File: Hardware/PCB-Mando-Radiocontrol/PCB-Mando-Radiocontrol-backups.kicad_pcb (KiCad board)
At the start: 2 copper layers, 132 x 66 mm, 25 parts, among them J1 USB 2.0 a UART TTL 6 pines CP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, J2 ALIMENTACION, SW1 SW_SPDT, SW2 SW_SPDT, SW3 SW_SPDT, U1 ATMEGA328P, U2 Nrf24l01, U3 AMS1117-3.3, U4 AMS1117-5.0, U5 COM-09032, U6 COM-09032, Y1 16MHZ

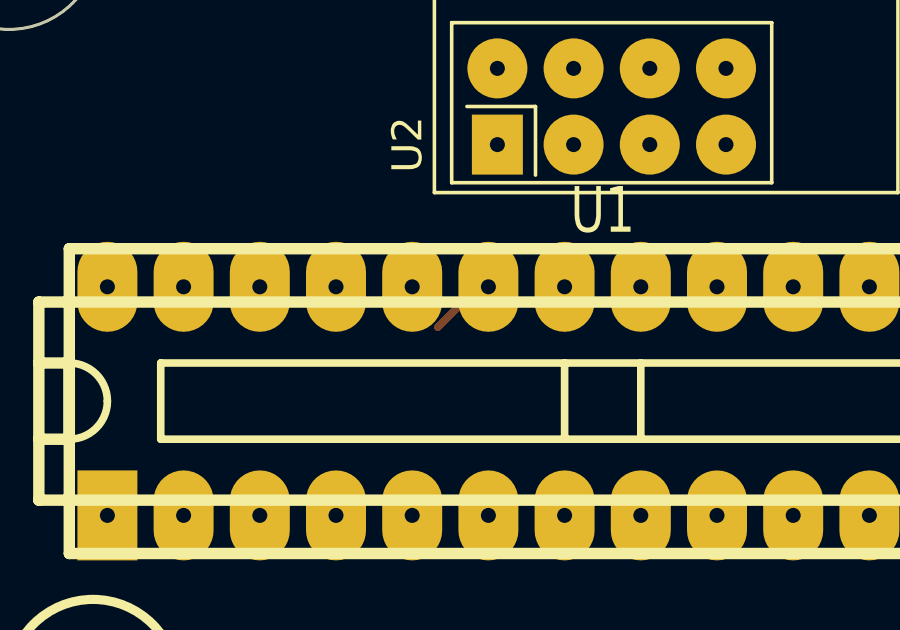
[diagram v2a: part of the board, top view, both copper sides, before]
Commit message: Errores en el esquematico corregidos
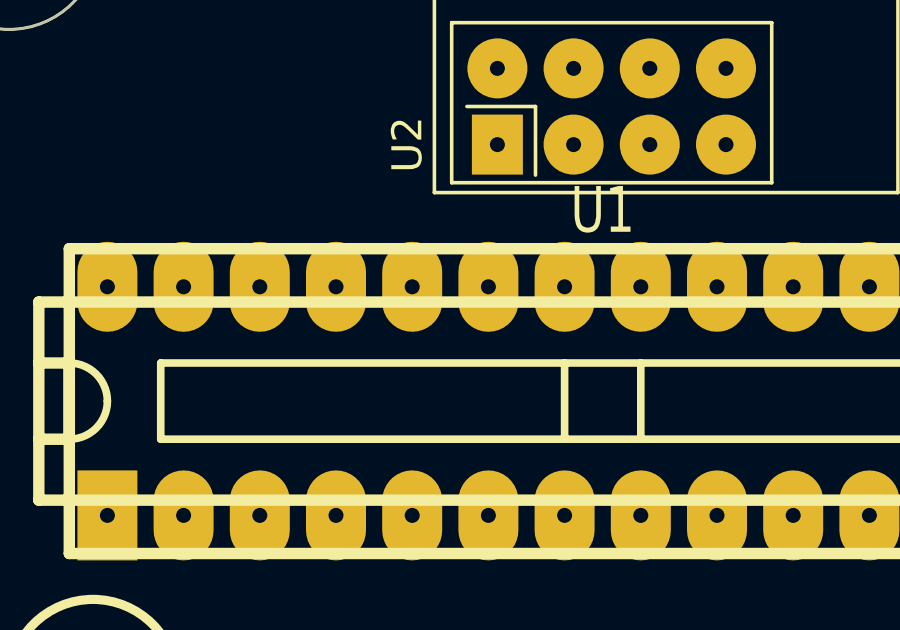
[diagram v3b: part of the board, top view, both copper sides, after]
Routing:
- net /PotIzqA: track 1.16 -> 0.00 mm
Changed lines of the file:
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@@
   )
   (setup
+    (stackup
+      (layer "F.SilkS" (type "Top Silk Screen"))
+      (layer "F.Paste" (type "Top Solder Paste"))
+      (layer "F.Mask" (type "Top Solder Mask") (thickness 0.01))
+      (layer "F.Cu" (type "copper") (thickness 0.035))
+      (layer "dielectric 1" (type "core") (thickness 1.51) (material "FR4") (epsilon_r 4.5) (loss_tangent 0.02))
+      (layer "B.Cu" (type "copper") (thickness 0.035))
+      (layer "B.Mask" (type "Bottom Solder Mask") (thickness 0.01))
+      (layer "B.Paste" (type "Bottom Solder Paste"))
+      (layer "B.SilkS" (type "Bottom Silk Screen"))
+      (copper_finish "None")
+      (dielectric_constraints no)
+    )
     (pad_to_mask_clearance 0)
     (pcbplotparams
@@
   (net 11 "/TX")
   (net 12 "unconnected-(J1-Pin_6-Pad6)")
-  (net 13 "unconnected-(SW2-A-Pad1)")
+  (net 13 "unconnected-(SW3-C-Pad3)")
   (net 14 "unconnected-(U1-D2-Pad4)")
   (net 15 "unconnected-(U1-D3-Pad5)")
@@
   (net 32 "unconnected-(U1-A5-Pad28)")
   (net 33 "unconnected-(U2-IRQ-Pad8)")
-  (net 34 "unconnected-(SW2-C-Pad3)")
-  (net 35 "unconnected-(SW3-A-Pad1)")
-  (net 36 "unconnected-(SW3-C-Pad3)")
+  (net 34 "unconnected-(SW3-A-Pad1)")
+  (net 35 "unconnected-(SW2-C-Pad3)")
+  (net 36 "unconnected-(SW2-A-Pad1)")
   (footprint "PotStick:XDCR_COM-09032" (layer "F.Cu")
     (at 113.84 98.84 90)
@@
       (stroke (width 0.15) (type solid)) (layer "F.SilkS"))
     (pad "1" thru_hole rect (at -2.54 0) (size 2 2.19964) (drill 0.5) (layers "*.Cu" "*.Mask" "F.SilkS")
-      (net 35 "unconnected-(SW3-A-Pad1)") (pinfunction "A") (pintype "passive"))
+      (net 34 "unconnected-(SW3-A-Pad1)") (pinfunction "A") (pintype "passive"))
     (pad "2" thru_hole oval (at 0 0) (size 2.2 2.19964) (drill 0.5) (layers "*.Cu" "*.Mask" "F.SilkS")
       (net 16 "/SwDer") (pinfunction "B") (pintype "passive"))
     (pad "3" thru_hole oval (at 2.54 0) (size 2 2.19964) (drill 0.5) (layers "*.Cu" "*.Mask" "F.SilkS")
-      (net 36 "unconnected-(SW3-C-Pad3)") (pinfunction "C") (pintype "passive"))
+      (net 13 "unconnected-(SW3-C-Pad3)") (pinfunction "C") (pintype "passive"))
     (model "Pin_socket_3.wrl"
       (offset (xyz 0 0 0))
@@
       (stroke (width 0.15) (type solid)) (layer "F.SilkS"))
     (pad "1" thru_hole rect (at -2.54 0) (size 2 2.19964) (drill 0.5) (layers "*.Cu" "*.Mask" "F.SilkS")
-      (net 13 "unconnected-(SW2-A-Pad1)") (pinfunction "A") (pintype "passive"))
+      (net 36 "unconnected-(SW2-A-Pad1)") (pinfunction "A") (pintype "passive"))
     (pad "2" thru_hole oval (at 0 0) (size 2 2.19964) (drill 0.5) (layers "*.Cu" "*.Mask" "F.SilkS")
       (net 17 "/SwIzq") (pinfunction "B") (pintype "passive"))
     (pad "3" thru_hole oval (at 2.54 0) (size 2 2.19964) (drill 0.5) (layers "*.Cu" "*.Mask" "F.SilkS")
-      (net 34 "unconnected-(SW2-C-Pad3)") (pinfunction "C") (pintype "passive"))
+      (net 35 "unconnected-(SW2-C-Pad3)") (pinfunction "C") (pintype "passive"))
     (model "Pin_socket_3.wrl"
       (offset (xyz 0 0 0))
@@
     (stroke (width 0.1) (type default)) (layer "Edge.Cuts"))
   (segment (start 174.25 112.5) (end 171.9 112.5) (width 0.25) (layer "F.Cu") (net 2))
-  (segment (start 151.29 97.93) (end 152.11 97.11) (width 0.25) (layer "F.Cu") (net 27))
 )

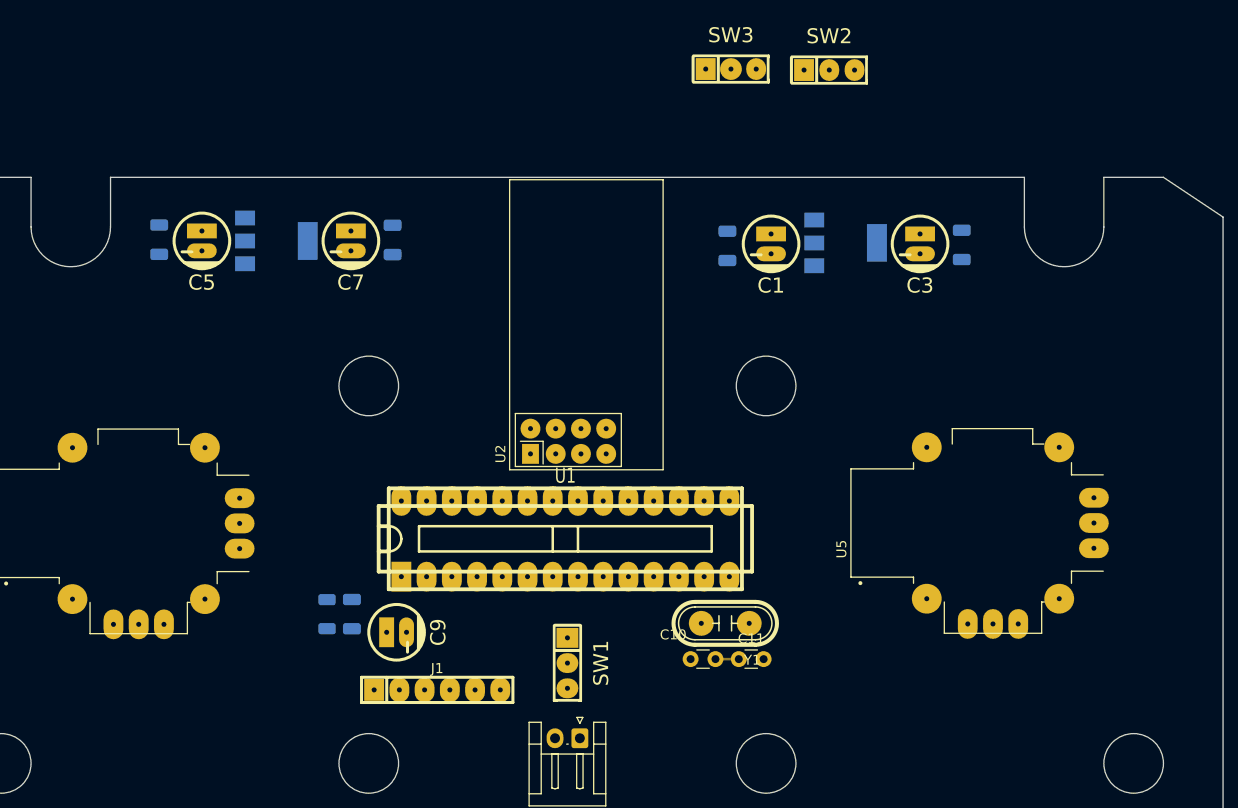
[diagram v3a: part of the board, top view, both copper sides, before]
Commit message: SCH corregido, PCB en proceso a falta de NRF
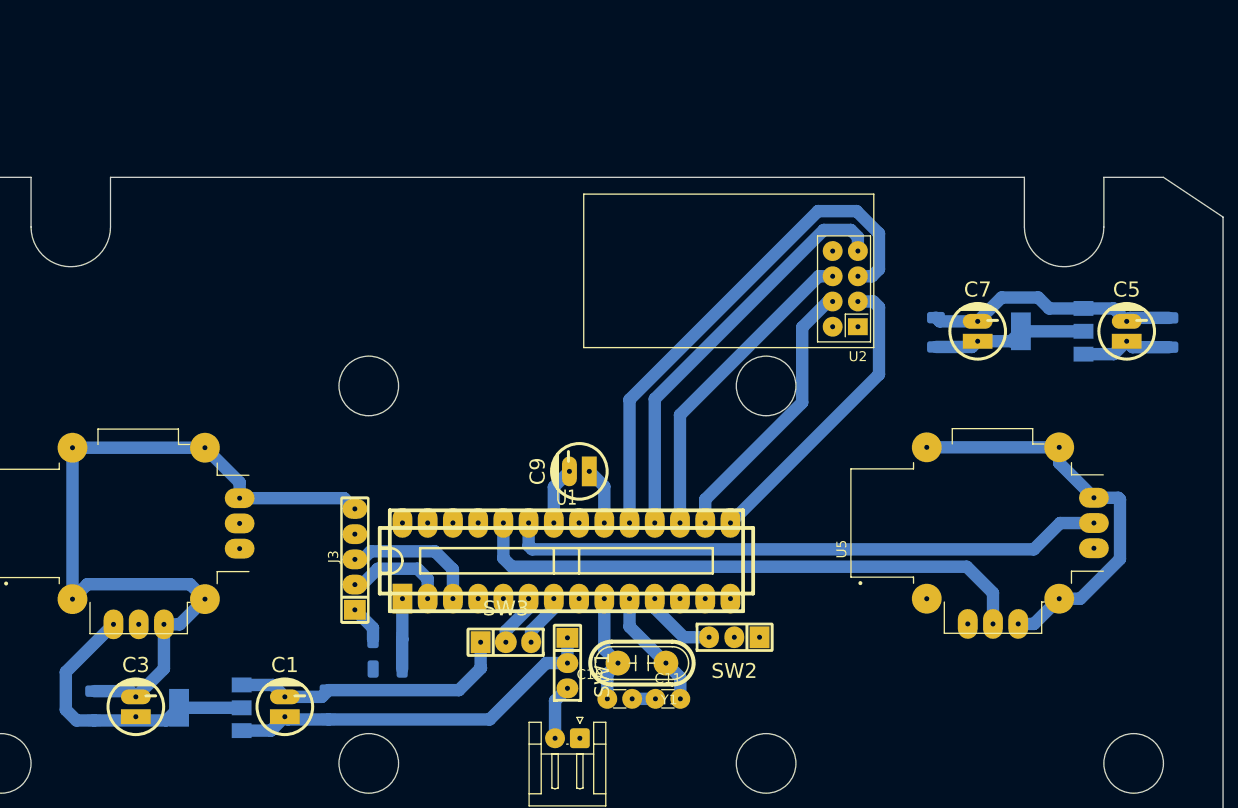
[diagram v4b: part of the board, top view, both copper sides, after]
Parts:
- removed J1: USB 2.0 a UART TTL 6 pines CP2102, EESTN5:Pin_Header_6
- added J3: USB 2.0 a UART TTL 6 pines CP2102, EESTN5:Pin_Header_5, F.Cu at (135.6, 102.5)
- moved C6 102.1 mm to (217.6, 79.6), turned to 90 degrees
- moved C4 98.9 mm to (109.3, 117.2), turned to 90 degrees
- moved C5 93.5 mm to (213.3, 79.5), turned to 0 degrees
- moved C3 91.7 mm to (113.5, 117.3), turned to 0 degrees
- moved U4 79.2 mm to (121.0, 117.4), turned to 180 degrees
- moved U3 78.6 mm to (205.8, 79.5), turned to 180 degrees
- moved C1 67.6 mm to (128.6, 117.3), turned to 0 degrees
- moved C7 63.8 mm to (198.3, 79.5), turned to 0 degrees
- moved SW3 62.0 mm to (150.8, 110.8)
- moved C2 61.2 mm to (132.9, 117.1), turned to 90 degrees
- moved SW2 57.9 mm to (173.8, 110.3), turned to 180 degrees
- moved C8 55.5 mm to (194.1, 79.6), turned to 90 degrees
- moved U2 35.4 mm to (186.2, 79.0), turned to 180 degrees
- moved C9 24.5 mm to (158.2, 93.6), turned to 90 degrees
- moved C10 9.29 mm to (163.5, 116.5)
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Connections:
- SW2 pad 1: unconnected-(SW2-A-Pad1) -> +5V
- SW2 pad 2: /SwIzq -> GND
- SW2 pad 3: unconnected-(SW2-C-Pad3) -> /SwIzq
- SW3 pad 1: unconnected-(SW3-A-Pad1) -> GND
- SW3 pad 3: unconnected-(SW3-C-Pad3) -> +5V
- U1 pad 23: /PotIzqA -> /PotDerA
- U1 pad 24: /PotIzqB -> /PotDerB
- U1 pad 25: /PotDerA -> /PotIzqB
- U1 pad 26: /PotDerB -> /PotIzqA
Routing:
- net GND: track 2.35 -> 183.7 mm
- net /PotDerA: track 0.00 -> 60.5 mm
- net /PotDerB: track 0.00 -> 57.4 mm
- net /SCK: track 0.00 -> 52.3 mm
- net VCC: track 0.00 -> 47.8 mm
- net /MISO: track 0.00 -> 41.7 mm
- net +5V: track 0.00 -> 40.4 mm
- net /MOSI: track 0.00 -> 32.0 mm
- net /CE: track 0.00 -> 30.3 mm
- net /CSK: track 0.00 -> 27.9 mm
- net +3V3: track 0.00 -> 15.5 mm
- net /TX: track 0.00 -> 13.9 mm
- net Net-(C11-Pad2): track 0.00 -> 12.2 mm
- net Net-(C10-Pad2): track 0.00 -> 11.1 mm
- net /RX: track 0.00 -> 10.4 mm
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
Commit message: SCH Completo, PCB en proceso en un ~80%
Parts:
- moved C6 52.3 mm to (180.8, 116.8), turned to -90 degrees
- moved C5 46.8 mm to (185.2, 116.9), turned to 180 degrees
- moved U3 39.6 mm to (192.7, 116.9), turned to 0 degrees
- moved C8 38.6 mm to (204.3, 116.8), turned to -90 degrees
- moved C7 37.4 mm to (200.2, 116.9), turned to 180 degrees
- moved U2 12.4 mm to (198.4, 81.4)
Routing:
- net +5V: track 40.4 -> 106.2 mm
- net /PotIzqB: track 0.00 -> 61.2 mm
- net VCC: track 47.8 -> 85.2 mm
- net /PotIzqA: track 0.00 -> 26.5 mm
- net /SCK: track 52.3 -> 71.2 mm
- net /MISO: track 41.7 -> 57.6 mm
- net /MOSI: track 32.0 -> 47.3 mm
- net /CSK: track 27.9 -> 42.1 mm
- net /CE: track 30.3 -> 42.9 mm
- net GND: track 183.7 -> 187.3 mm
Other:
- outline, holes or cut-outs redrawn

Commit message: SCH completo, PCB en proceso ~90% completado
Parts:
- moved J3 9.12 mm to (131.3, 110.5), turned to 180 degrees
- moved C12 1.43 mm to (140.3, 110.6)
- moved R5 1.43 mm to (140.3, 113.6)
- moved C9 0.81 mm to (158.1, 92.8), turned to 180 degrees
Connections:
- U5 pad S1: GND -> Net-(U5-SHIELD-PadS1)
- U5 pad S2: GND -> Net-(U5-SHIELD-PadS1)
- U5 pad S3: GND -> Net-(U5-SHIELD-PadS1)
- U5 pad S4: GND -> Net-(U5-SHIELD-PadS1)
- U6 pad S1: GND -> Net-(U6-SHIELD-PadS1)
- U6 pad S2: GND -> Net-(U6-SHIELD-PadS1)
- U6 pad S3: GND -> Net-(U6-SHIELD-PadS1)
- U6 pad S4: GND -> Net-(U6-SHIELD-PadS1)
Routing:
- net +5V: track 106.2 -> 347.6 mm, vias 0 -> 3
- net +3V3: track 15.5 -> 65.7 mm, vias 0 -> 1
- net GND: track 187.3 -> 217.9 mm, vias 0 -> 1
- net /PotIzqB: track 61.2 -> 49.6 mm
- net /TX: track 13.9 -> 23.4 mm
- net /RX: track 10.4 -> 16.3 mm
- net /DTR: track 3.72 -> 2.51 mm
- net Net-(U1-Reset): track 7.10 -> 7.77 mm
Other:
- outline, holes or cut-outs redrawn

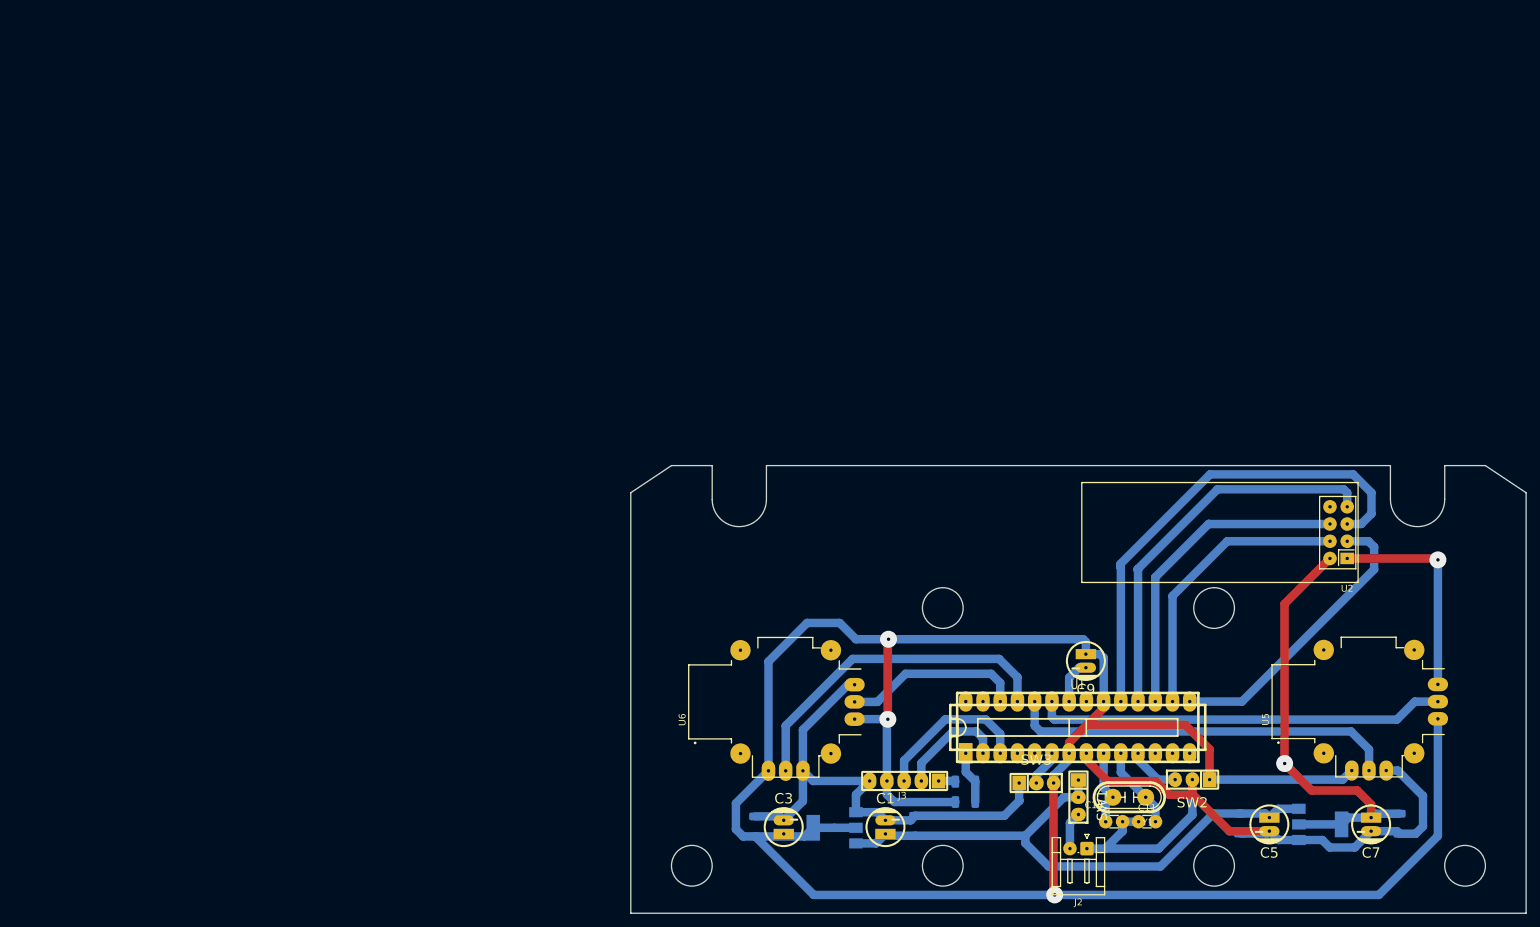
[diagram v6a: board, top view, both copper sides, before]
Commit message: realice modificaciones desde 0 en el PCB a continuar por leandro, es una placa en paralelo a la de gabi
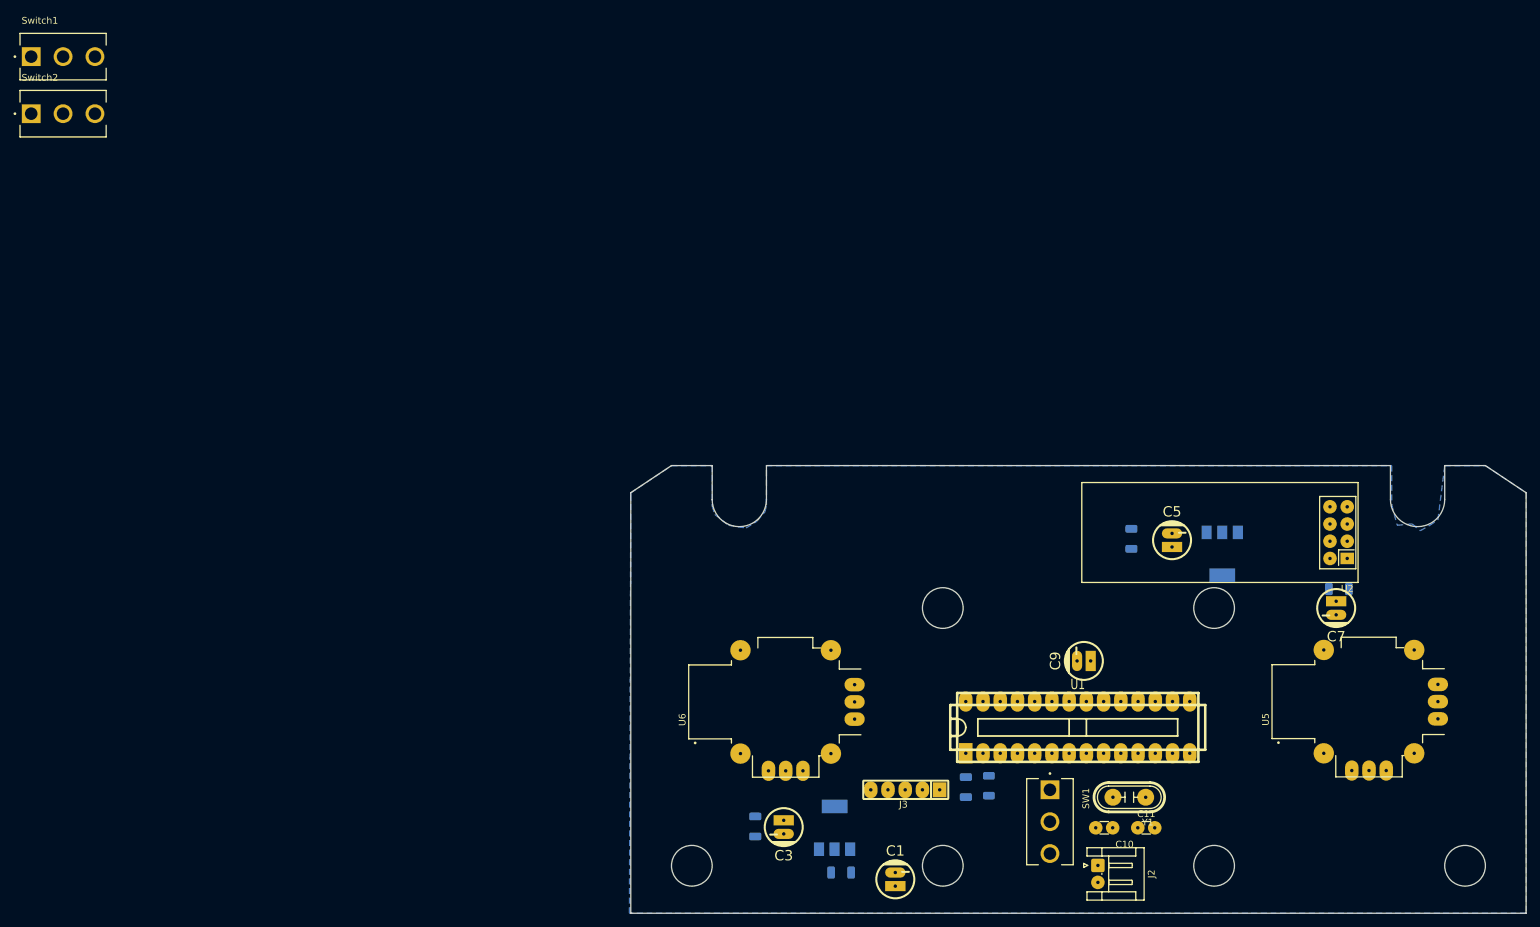
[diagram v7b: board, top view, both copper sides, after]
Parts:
- removed SW2, SW3: SW_SPDT, EESTN5:Pin_Header_3
- added Switch1: ~, Footprints:SW_100SP3T1B1M2QE, F.Cu at (7.30, 3.71)
- added Switch2: ~, Footprints:SW_100SP3T1B1M2QE, F.Cu at (7.30, 12.1)
- SW1: footprint EESTN5:Pin_Header_3 -> Footprints:SW_100SP3T1B1M2QE
- moved C6 44.9 mm to (164.8, 74.8), turned to 90 degrees
- moved C5 44.3 mm to (170.8, 75.0), turned to 0 degrees
- moved U3 42.4 mm to (178.2, 77.0), turned to -90 degrees
- moved C8 35.7 mm to (195.4, 82.2), turned to 0 degrees
- moved C7 32.3 mm to (195.0, 85.0)
- moved C2 12.9 mm to (122.0, 124.0), turned to 0 degrees
- moved C1 7.84 mm to (130.0, 125.0)
- moved SW1 5.53 mm to (152.8, 116.5)
- moved R5 4.22 mm to (143.8, 111.2), turned to 90 degrees
- moved C10 4.06 mm to (159.6, 117.4), turned to 0 degrees
- moved J2 2.96 mm to (159.9, 123.0), turned to -90 degrees
- moved J3 1.31 mm to (131.5, 111.8)
- moved C11 0.91 mm to (165.8, 117.4)
- moved C12 0.80 mm to (140.4, 111.4), turned to -90 degrees
- moved C9 0.30 mm to (157.8, 92.8), turned to 90 degrees
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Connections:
- C5 pad 1: VCC -> +5V
- C6 pad 1: VCC -> +5V
- U1 pad 11: /SwIzq -> unconnected-(U1-D5-Pad11)
- U1 pad 6: /SwDer -> unconnected-(U1-D4-Pad6)
- U3 pad 3: VCC -> +5V
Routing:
- net +5V: track 347.6 -> 0.97 mm, vias 3 -> 0
- net GND: track 217.9 -> 0.00 mm, vias 1 -> 0
- net VCC: track 85.2 -> 0.00 mm
- net /SCK: track 71.2 -> 0.00 mm
- net +3V3: track 65.7 -> 0.00 mm, vias 1 -> 0
- net /PotDerA: track 60.5 -> 0.00 mm
- net /MISO: track 57.6 -> 0.00 mm
- net /PotDerB: track 57.4 -> 0.00 mm
- net /PotIzqB: track 49.6 -> 0.00 mm
- net /MOSI: track 47.3 -> 0.00 mm
- net /CE: track 42.9 -> 0.00 mm
- net /CSK: track 42.1 -> 0.00 mm
- net /PotIzqA: track 26.5 -> 0.00 mm
- net /TX: track 23.4 -> 0.00 mm
- net /RX: track 16.3 -> 0.00 mm
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- added copper zone on B.Cu, net GND
